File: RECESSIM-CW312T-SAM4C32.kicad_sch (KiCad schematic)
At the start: 100 parts

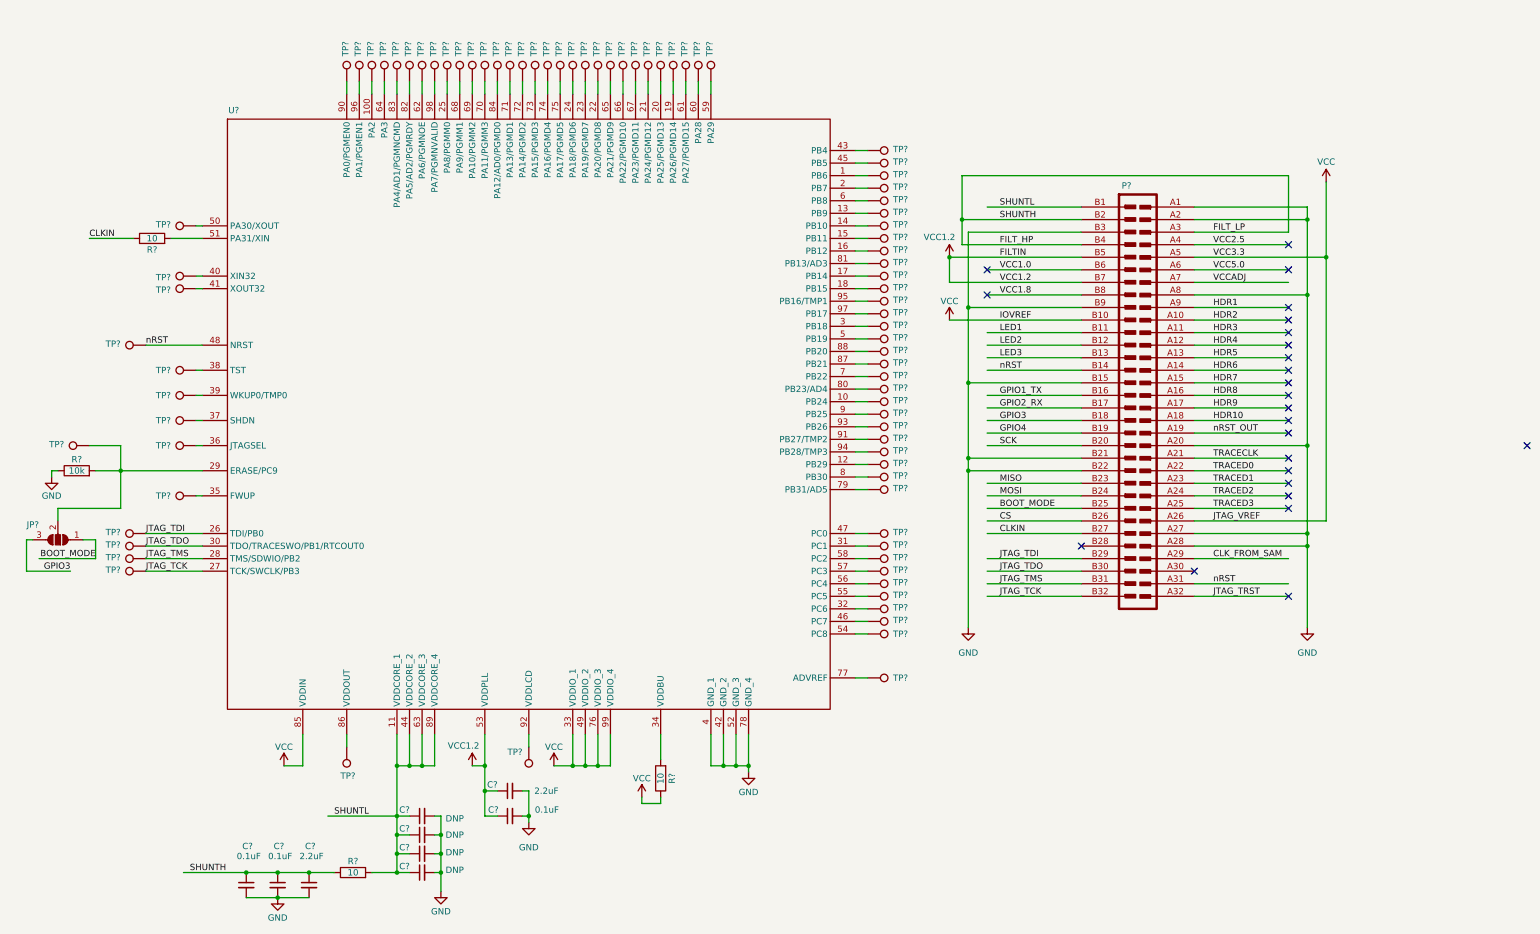
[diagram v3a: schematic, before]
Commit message: Added CW312T card edge footprint, finalized schematic before annotating
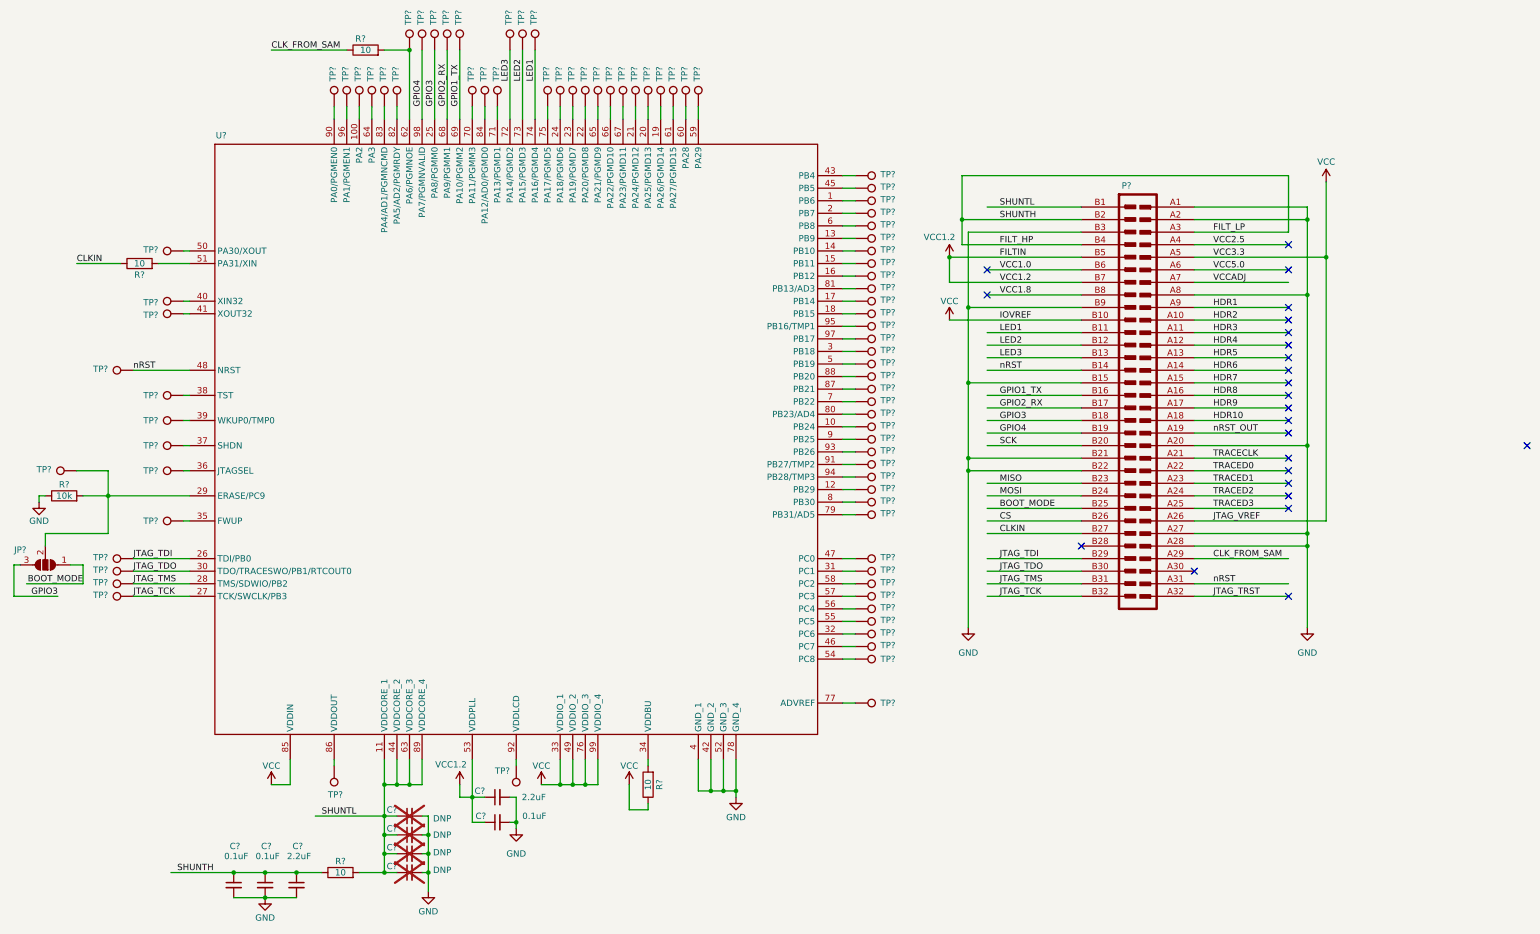
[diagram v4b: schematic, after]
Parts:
- added R?: 10, Resistor_SMD:R_0603_1608Metric, symbol Device:R
- C? (x5): footprint (none) -> Capacitor_SMD:C_0603_1608Metric
- C? (x4): footprint (none) -> Capacitor_SMD:C_0603_1608Metric; now not fitted
- JP?: footprint (none) -> Jumper:SolderJumper-3_P1.3mm_Open_RoundedPad1.0x1.5mm
- P?: footprint (none) -> RECESSIM-CW312T-SAM4C32:CW312_CardEdge
- R? (x4): footprint (none) -> Resistor_SMD:R_0603_1608Metric
- TP? (x84): footprint (none) -> TestPoint:TestPoint_Pad_1.0x1.0mm
- U?: footprint (none) -> Package_QFP:TQFP-100_14x14mm_P0.5mm
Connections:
- net CLK_FROM_SAM: now also R?.1
- net GPIO1_TX: now also TP?.1, U?.69 (PA10/PGMM2)
- net GPIO2_RX: now also TP?.1, U?.68 (PA9/PGMM1)
- net GPIO3: now also TP?.1, U?.25 (PA8/PGMM0)
- net GPIO4: now also TP?.1, U?.98 (PA7/PGMNVALID)
- net LED1: now also TP?.1, U?.74 (PA16/PGMD4)
- net LED2: now also TP?.1, U?.73 (PA15/PGMD3)
- net LED3: now also TP?.1, U?.72 (PA14/PGMD2)
- net at TP?.1, U?.62 (PA6/PGMNOE): now also R?.2
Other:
- moved on the sheet: C?, JP?, R?, TP?, U?

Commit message: Updated schematic footprint, annotated and ran DRC
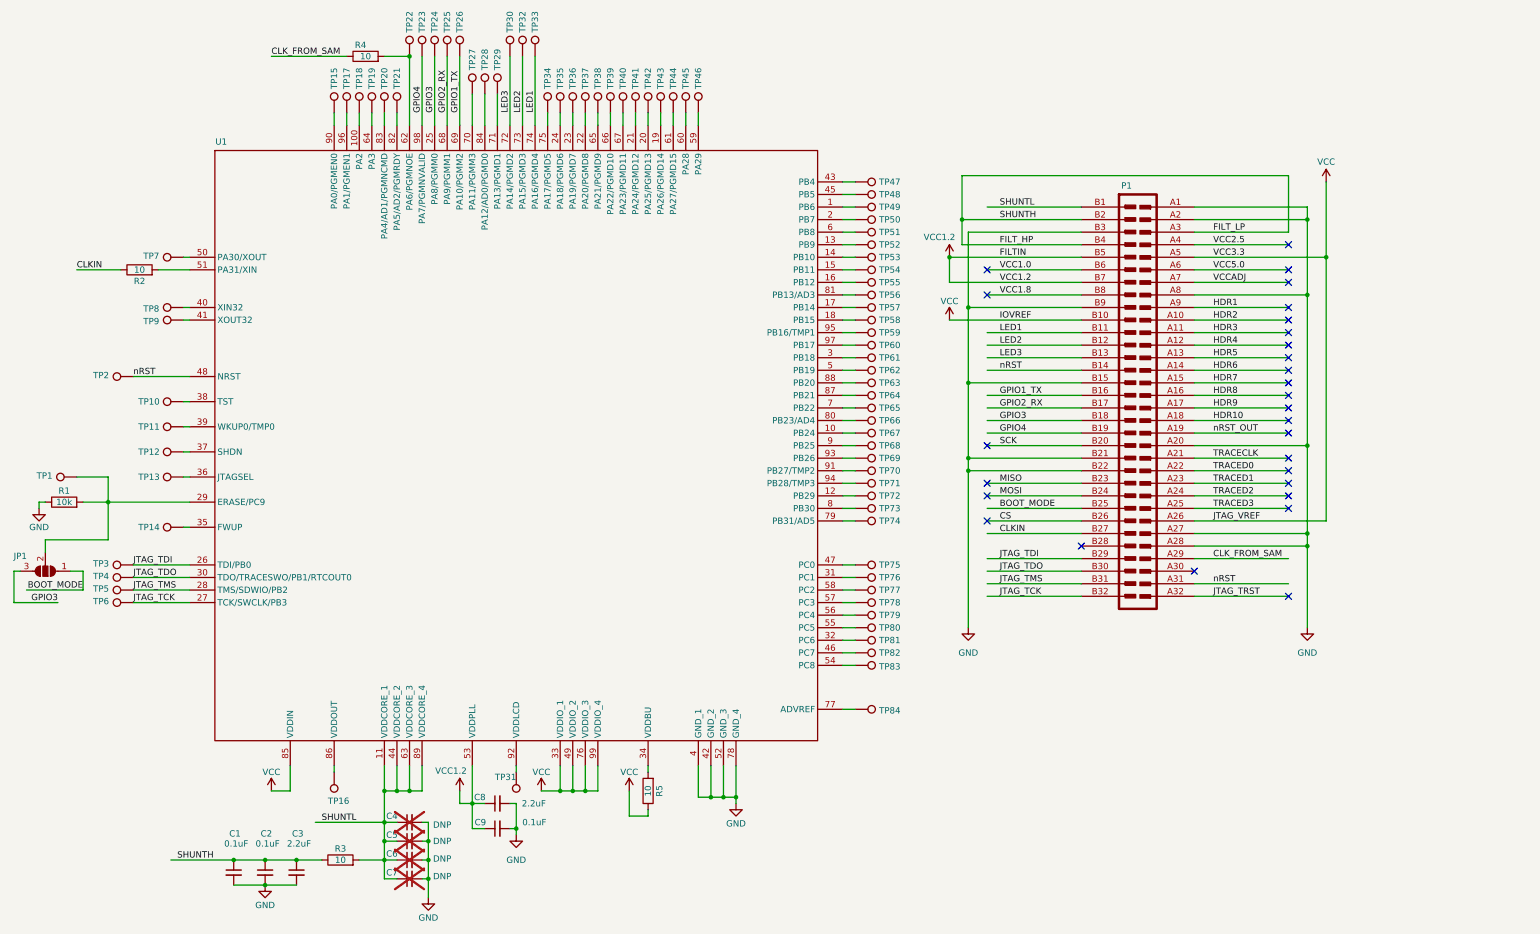
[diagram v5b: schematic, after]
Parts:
- gave numbers to parts that had none: 101
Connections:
- no-connect marks 24 -> 28
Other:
- moved on the sheet: C1, C2, C3, C4, C5, C6, C7, C8, C9, JP1, R1, R2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

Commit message: Updated footprints for card edge and initial placement of components on board
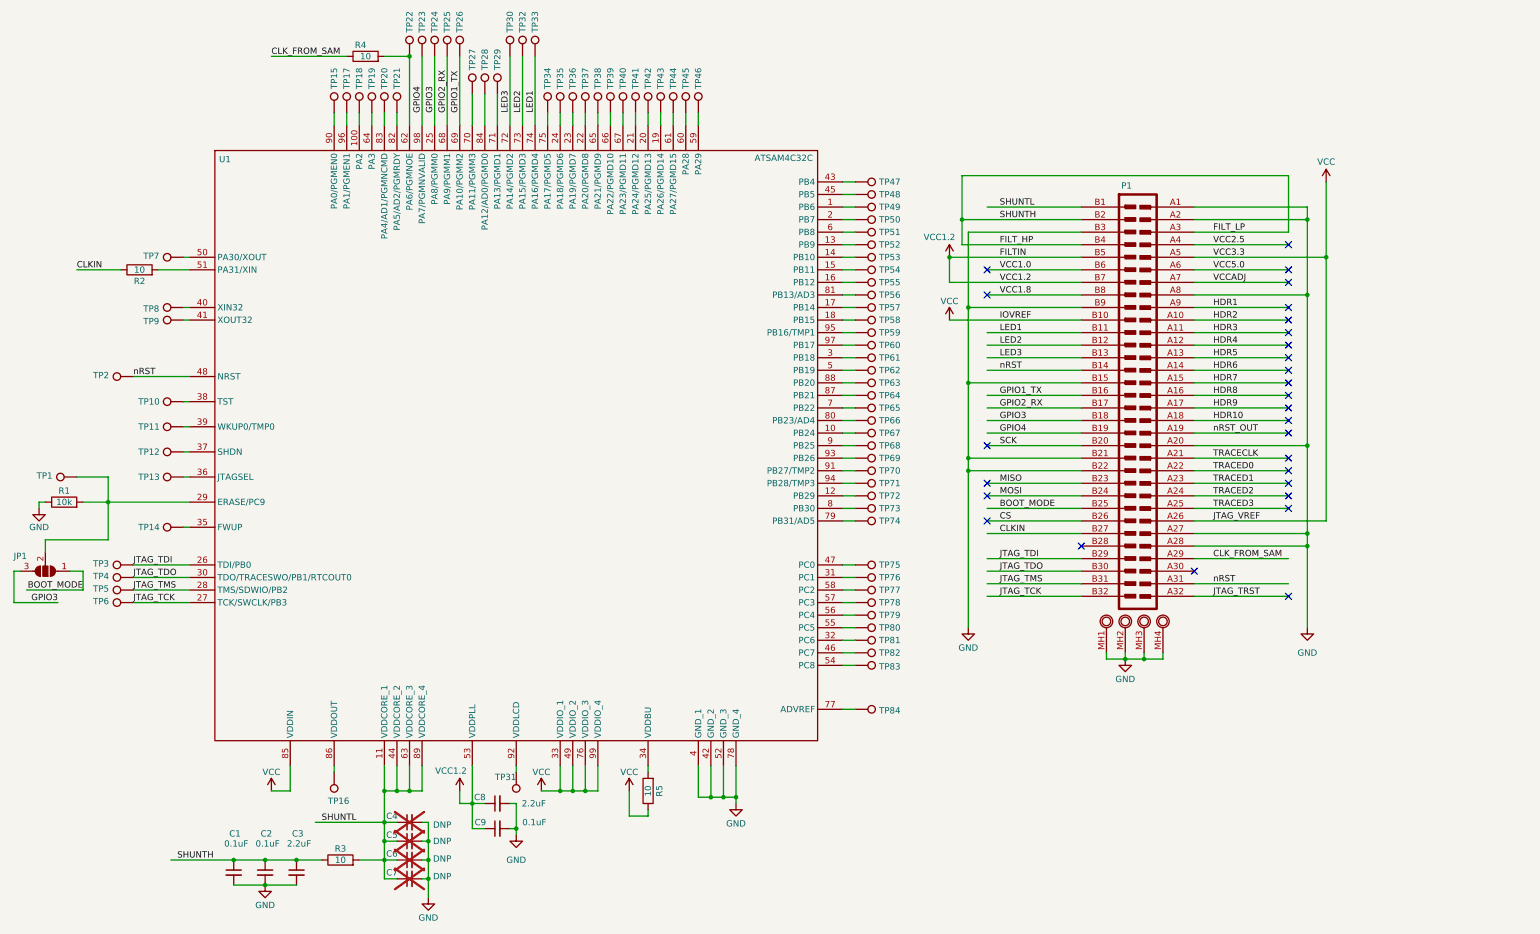
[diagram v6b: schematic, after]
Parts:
- U1: value ~ -> ATSAM4C32C
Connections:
- net GND: now also P1.MH1 (MH), P1.MH2 (MH), P1.MH3 (MH), P1.MH4 (MH)

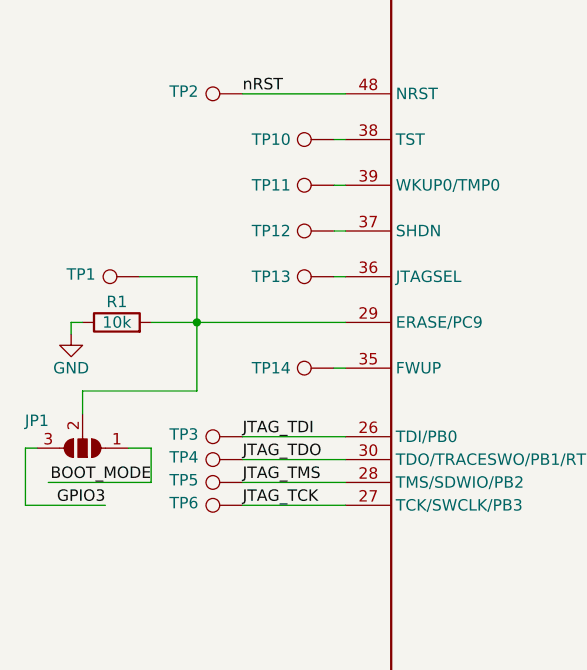
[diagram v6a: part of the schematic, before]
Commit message: Added two necessary resistors and removed one unnecessary one
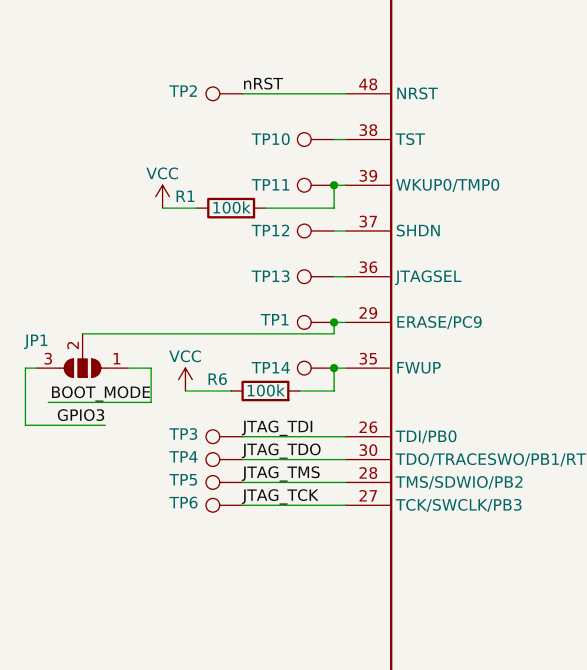
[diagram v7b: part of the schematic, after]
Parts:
- added R6: 100k, Resistor_SMD:R_0603_1608Metric, symbol Device:R
- R1: value 10k -> 100k
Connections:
- net GND: no longer R1.1
- net VCC: now also R1.1, R6.1
- net at JP1.2 (C), TP1.1, U1.29 (ERASE/PC9): no longer R1.2
- net at TP14.1, U1.35 (FWUP): now also R6.2
- net at TP11.1, U1.39 (WKUP0/TMP0): now also R1.2
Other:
- moved on the sheet: JP1, TP1

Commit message: Finalized PCB design, generated gerbers for version 1
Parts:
- renumbered C8 to C4, C9 to C5, C4 to C6, C5 to C8, C6 to C9, R4 to R1, R5 to R4, R6 to R5, R1 to R6, TP6 to TP1, TP16 to TP11, TP11 to TP12, TP8 to TP13, TP9 to TP14, TP2 to TP15, TP7 to TP16, TP5 to TP2, TP4 to TP3, TP3 to TP4, TP1 to TP5, TP14 to TP6, TP13 to TP7, TP12 to TP8, TP31 to TP9
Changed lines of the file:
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@@
 		(on_board yes)
 		(dnp no)
-		(property "Reference" "TP4"
+		(property "Reference" "TP3"
 			(at 31.242 126.746 90)
 			(effects
@@
 			(project "RECESSIM-CW312T-SAM4C32"
 				(path "/669e0635-14d7-44ae-ae87-da7f613321c5"
-					(reference "TP4")
+					(reference "TP3")
 					(unit 1)
 				)
@@
 		(on_board yes)
 		(dnp no)
-		(property "Reference" "TP6"
+		(property "Reference" "TP1"
 			(at 31.242 131.826 90)
 			(effects
@@
 			(project "RECESSIM-CW312T-SAM4C32"
 				(path "/669e0635-14d7-44ae-ae87-da7f613321c5"
-					(reference "TP6")
+					(reference "TP1")
 					(unit 1)
 				)
@@
 		(on_board yes)
 		(dnp no)
-		(property "Reference" "TP5"
+		(property "Reference" "TP2"
 			(at 31.242 129.286 90)
 			(effects
@@
 			(project "RECESSIM-CW312T-SAM4C32"
 				(path "/669e0635-14d7-44ae-ae87-da7f613321c5"
-					(reference "TP5")
+					(reference "TP2")
 					(unit 1)
 				)
@@
 		(on_board yes)
 		(dnp no)
-		(property "Reference" "C9"
+		(property "Reference" "C5"
 			(at 110.744 176.53 90)
 			(effects
@@
 			(project ""
 				(path "/669e0635-14d7-44ae-ae87-da7f613321c5"
-					(reference "C9")
+					(reference "C5")
 					(unit 1)
 				)
@@
 		(on_board yes)
 		(dnp no)
-		(property "Reference" "TP12"
+		(property "Reference" "TP8"
 			(at 40.386 101.6 90)
 			(effects
@@
 			(project "RECESSIM-CW312T-SAM4C32"
 				(path "/669e0635-14d7-44ae-ae87-da7f613321c5"
-					(reference "TP12")
+					(reference "TP8")
 					(unit 1)
 				)
@@
 		(on_board yes)
 		(dnp yes)
-		(property "Reference" "C4"
+		(property "Reference" "C6"
 			(at 91.694 175.26 90)
 			(effects
@@
 			(project "RECESSIM-CW312T-SAM4C32"
 				(path "/669e0635-14d7-44ae-ae87-da7f613321c5"
-					(reference "C4")
+					(reference "C6")
 					(unit 1)
 				)
@@
 		(on_board yes)
 		(dnp no)
-		(property "Reference" "TP3"
+		(property "Reference" "TP4"
 			(at 31.242 124.206 90)
 			(effects
@@
 			(project "RECESSIM-CW312T-SAM4C32"
 				(path "/669e0635-14d7-44ae-ae87-da7f613321c5"
-					(reference "TP3")
+					(reference "TP4")
 					(unit 1)
 				)
@@
 		(on_board yes)
 		(dnp no)
-		(property "Reference" "TP14"
+		(property "Reference" "TP6"
 			(at 40.386 116.84 90)
 			(effects
@@
 			(project "RECESSIM-CW312T-SAM4C32"
 				(path "/669e0635-14d7-44ae-ae87-da7f613321c5"
-					(reference "TP14")
+					(reference "TP6")
 					(unit 1)
 				)
@@
 		(on_board yes)
 		(dnp no)
-		(property "Reference" "TP16"
+		(property "Reference" "TP11"
 			(at 78.74 172.212 0)
 			(effects
@@
 			(project ""
 				(path "/669e0635-14d7-44ae-ae87-da7f613321c5"
-					(reference "TP16")
+					(reference "TP11")
 					(unit 1)
 				)
@@
 		(on_board yes)
 		(dnp no)
-		(property "Reference" "TP13"
+		(property "Reference" "TP7"
 			(at 40.386 106.68 90)
 			(effects
@@
 			(project "RECESSIM-CW312T-SAM4C32"
 				(path "/669e0635-14d7-44ae-ae87-da7f613321c5"
-					(reference "TP13")
+					(reference "TP7")
 					(unit 1)
 				)
@@
 		(on_board yes)
 		(dnp yes)
-		(property "Reference" "C5"
+		(property "Reference" "C8"
 			(at 91.694 179.07 90)
 			(effects
@@
 			(project "RECESSIM-CW312T-SAM4C32"
 				(path "/669e0635-14d7-44ae-ae87-da7f613321c5"
-					(reference "C5")
+					(reference "C8")
 					(unit 1)
 				)
@@
 		(on_board yes)
 		(dnp no)
-		(property "Reference" "TP2"
+		(property "Reference" "TP15"
 			(at 31.242 86.106 90)
 			(effects
@@
 			(project "RECESSIM-CW312T-SAM4C32"
 				(path "/669e0635-14d7-44ae-ae87-da7f613321c5"
-					(reference "TP2")
+					(reference "TP15")
 					(unit 1)
 				)
@@
 		(on_board yes)
 		(dnp no)
-		(property "Reference" "R5"
+		(property "Reference" "R4"
 			(at 145.796 170.18 90)
 			(effects
@@
 			(project "RECESSIM-CW312T-SAM4C32"
 				(path "/669e0635-14d7-44ae-ae87-da7f613321c5"
-					(reference "R5")
+					(reference "R4")
 					(unit 1)
 				)
@@
 		(on_board yes)
 		(dnp no)
-		(property "Reference" "R6"
+		(property "Reference" "R5"
 			(at 36.576 118.11 90)
 			(effects
@@
 			(project "RECESSIM-CW312T-SAM4C32"
 				(path "/669e0635-14d7-44ae-ae87-da7f613321c5"
-					(reference "R6")
+					(reference "R5")
 					(unit 1)
 				)
@@
 		(on_board yes)
 		(dnp no)
-		(property "Reference" "R1"
+		(property "Reference" "R6"
 			(at 33.02 97.79 90)
 			(effects
@@
 			(project "RECESSIM-CW312T-SAM4C32"
 				(path "/669e0635-14d7-44ae-ae87-da7f613321c5"
-					(reference "R1")
+					(reference "R6")
 					(unit 1)
 				)
@@
 		(on_board yes)
 		(dnp no)
-		(property "Reference" "TP1"
+		(property "Reference" "TP5"
 			(at 41.402 111.506 90)
 			(effects
@@
 			(project "RECESSIM-CW312T-SAM4C32"
 				(path "/669e0635-14d7-44ae-ae87-da7f613321c5"
-					(reference "TP1")
+					(reference "TP5")
 					(unit 1)
 				)
@@
 		(on_board yes)
 		(dnp no)
-		(property "Reference" "TP8"
+		(property "Reference" "TP13"
 			(at 41.402 72.644 90)
 			(effects
@@
 			(project "RECESSIM-CW312T-SAM4C32"
 				(path "/669e0635-14d7-44ae-ae87-da7f613321c5"
-					(reference "TP8")
+					(reference "TP13")
 					(unit 1)
 				)
@@
 		(on_board yes)
 		(dnp no)
-		(property "Reference" "R4"
+		(property "Reference" "R1"
 			(at 85.344 19.304 90)
 			(effects
@@
 			(project "RECESSIM-CW312T-SAM4C32"
 				(path "/669e0635-14d7-44ae-ae87-da7f613321c5"
-					(reference "R4")
+					(reference "R1")
 					(unit 1)
 				)
@@
 		(on_board yes)
 		(dnp no)
-		(property "Reference" "C8"
+		(property "Reference" "C4"
 			(at 109.474 171.45 90)
 			(effects
@@
 			(project "RECESSIM-CW312T-SAM4C32"
 				(path "/669e0635-14d7-44ae-ae87-da7f613321c5"
-					(reference "C8")
+					(reference "C4")
 					(unit 1)
 				)
@@
 		(on_board yes)
 		(dnp no)
-		(property "Reference" "TP11"
+		(property "Reference" "TP12"
 			(at 40.386 96.52 90)
 			(effects
@@
 			(project "RECESSIM-CW312T-SAM4C32"
 				(path "/669e0635-14d7-44ae-ae87-da7f613321c5"
-					(reference "TP11")
+					(reference "TP12")
 					(unit 1)
 				)
@@
 		(on_board yes)
 		(dnp no)
-		(property "Reference" "TP7"
+		(property "Reference" "TP16"
 			(at 41.402 61.976 90)
 			(effects
@@
 			(project "RECESSIM-CW312T-SAM4C32"
 				(path "/669e0635-14d7-44ae-ae87-da7f613321c5"
-					(reference "TP7")
+					(reference "TP16")
 					(unit 1)
 				)
@@
 		(on_board yes)
 		(dnp yes)
-		(property "Reference" "C6"
+		(property "Reference" "C9"
 			(at 91.694 182.88 90)
 			(effects
@@
 			(project "RECESSIM-CW312T-SAM4C32"
 				(path "/669e0635-14d7-44ae-ae87-da7f613321c5"
-					(reference "C6")
+					(reference "C9")
 					(unit 1)
 				)
@@
 		(on_board yes)
 		(dnp no)
-		(property "Reference" "TP9"
+		(property "Reference" "TP14"
 			(at 41.402 75.184 90)
 			(effects
@@
 			(project "RECESSIM-CW312T-SAM4C32"
 				(path "/669e0635-14d7-44ae-ae87-da7f613321c5"
-					(reference "TP9")
+					(reference "TP14")
 					(unit 1)
 				)
@@
 		(on_board yes)
 		(dnp no)
-		(property "Reference" "TP31"
+		(property "Reference" "TP9"
 			(at 112.522 167.386 0)
 			(effects
@@
 			(project "RECESSIM-CW312T-SAM4C32"
 				(path "/669e0635-14d7-44ae-ae87-da7f613321c5"
-					(reference "TP31")
+					(reference "TP9")
 					(unit 1)
 				)
